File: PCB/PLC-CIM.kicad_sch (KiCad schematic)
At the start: 3 parts, among them J8 750678-1, U1 ESP32-DEVKITC

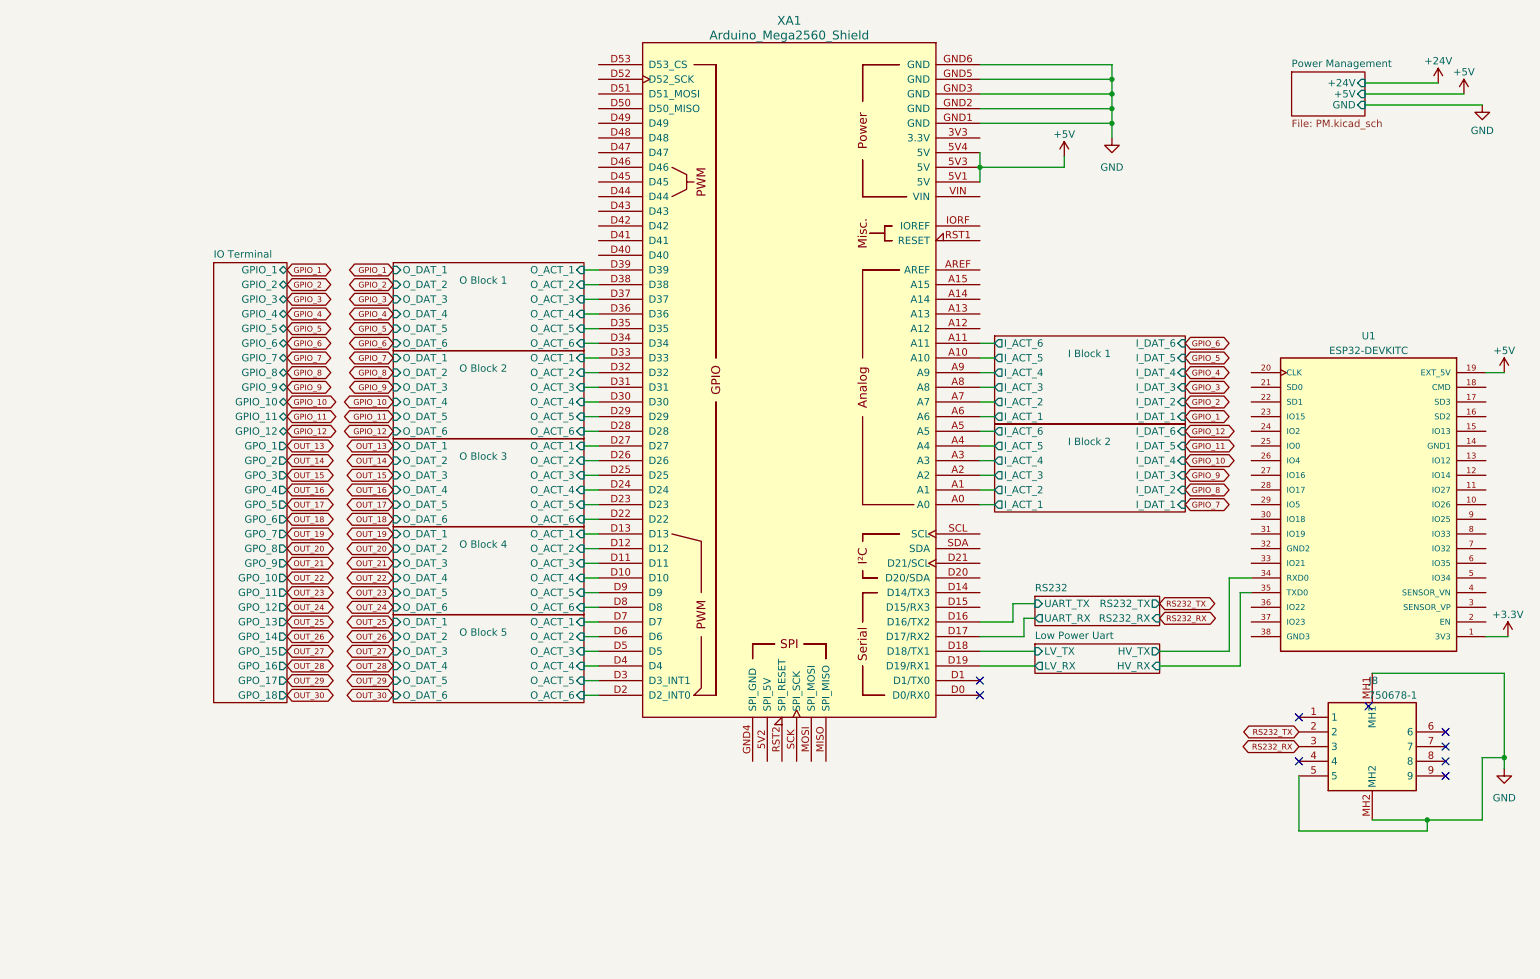
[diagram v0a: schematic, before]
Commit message: Redesigned, to utilize the ESP32 as the basis
* Implemented EEPROM
* Implemented RTC
* Implemented RS232 and 485
* Implemented CANBus
* Implemented everything
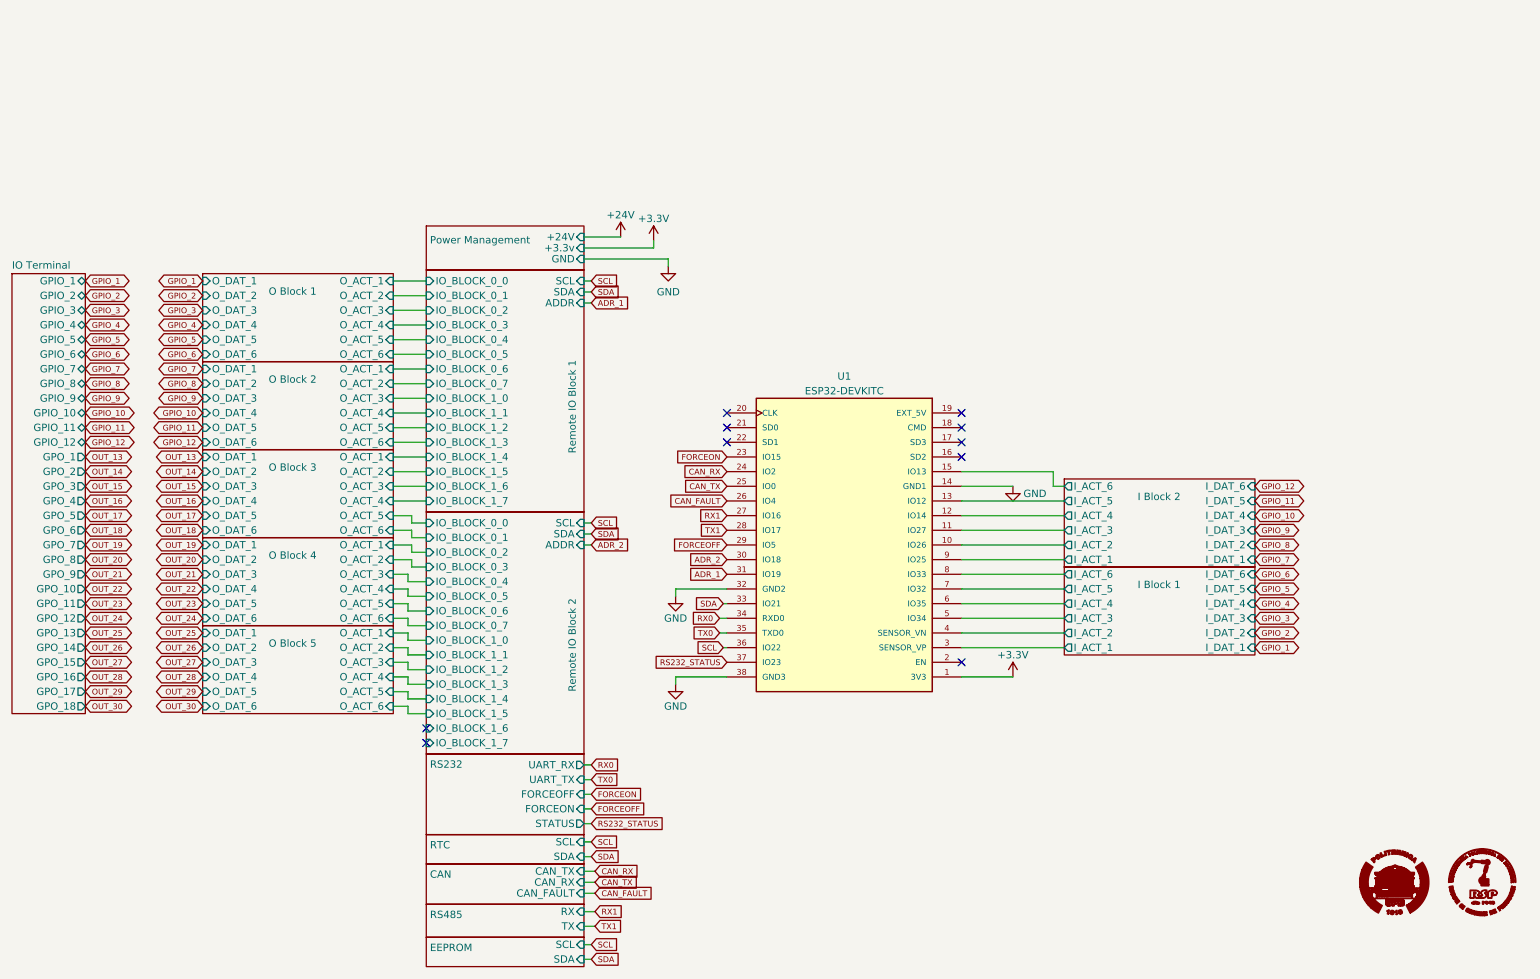
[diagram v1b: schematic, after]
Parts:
- removed J8: 750678-1, 7506781, symbol 750678-1:750678-1
- removed XA1: Arduino_Mega2560_Shield, PCM_arduino-library:Arduino_Mega2560_Shield, symbol arduino-library:Arduino_Mega2560_Shield
- U1: footprint MODULE_ESP32-DEVKITC -> SnapEDA Library:MODULE_ESP32-DEVKITC
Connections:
- net GND: now also U1.14 (GND1), U1.32 (GND2), U1.38 (GND3)
- net I Block 1/I_ACT_1: now also U1.3 (SENSOR_VP)
- net I Block 1/I_ACT_2: now also U1.4 (SENSOR_VN)
- net I Block 1/I_ACT_3: now also U1.5 (IO34)
- net I Block 1/I_ACT_4: now also U1.6 (IO35)
- net I Block 1/I_ACT_5: now also U1.7 (IO32)
- net I Block 1/I_ACT_6: now also U1.8 (IO33)
- net I Block 2/I_ACT_1: now also U1.9 (IO25)
- net I Block 2/I_ACT_2: now also U1.10 (IO26)
- net I Block 2/I_ACT_3: now also U1.11 (IO27)
- net I Block 2/I_ACT_4: now also U1.12 (IO14)
- net I Block 2/I_ACT_5: now also U1.13 (IO12)
- net I Block 2/I_ACT_6: now also U1.15 (IO13)
- net FORCEON: now reaches U1.23 (IO15)
- net CAN_RX: now reaches U1.24 (IO2)
- net CAN_TX: now reaches U1.25 (IO0)
- net CAN_FAULT: now reaches U1.26 (IO4)
- net RX1: now reaches U1.27 (IO16)
- net TX1: now reaches U1.28 (IO17)
- net FORCEOFF: now reaches U1.29 (IO5)
- net ADR_2: now reaches U1.30 (IO18)
- net ADR_1: now reaches U1.31 (IO19)
- net SDA: now reaches U1.33 (IO21)
- net SCL: now reaches U1.36 (IO22)
- net RS232_STATUS: now reaches U1.37 (IO23)
- net +5V: no longer names the net of U1.19 (EXT_5V)
- net Low Power Uart/HV_RX renamed TX0
- net Low Power Uart/HV_TX renamed RX0
- no-connect marks 9 -> 10
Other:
- removed sheet Low Power Uart
- added sheet CAN (CanXCIEVER.kicad_sch)
- added sheet EEPROM (EEPROM.kicad_sch)
- added sheet RS485 (RS485.kicad_sch)
- added sheet RTC (RTC.kicad_sch)
- added sheet Remote IO Block 1 (remoteIOBlock.kicad_sch)
- added sheet Remote IO Block 2 (remoteIOBlock.kicad_sch)
- sheet Power Management ports: added +3.3v; removed +5V
- sheet RS232 ports: added FORCEOFF, FORCEON, STATUS; removed RS232_RX, RS232_TX
- company: (none) -> UPB - FIIR - Roboți și sisteme de producție
- title: (none) -> PLC CIM

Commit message: Finalized PCB
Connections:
- net I Block 1/I_ACT_1 renamed MCU_IN_2
- net I Block 1/I_ACT_2 renamed MCU_IN_1
- net I Block 1/I_ACT_3 renamed MCU_IN_7
- net I Block 1/I_ACT_4 renamed MCU_IN_6
- net I Block 1/I_ACT_5 renamed MCU_IN_5
- net I Block 1/I_ACT_6 renamed MCU_IN_4
- net I Block 2/I_ACT_1 renamed MCU_IN_3
- net I Block 2/I_ACT_2 renamed MCU_IN_8
- net I Block 2/I_ACT_3 renamed MCU_IN_9
- net I Block 2/I_ACT_4 renamed MCU_IN_10
- net I Block 2/I_ACT_5 renamed MCU_IN_11
- net I Block 2/I_ACT_6 renamed MCU_IN_12
